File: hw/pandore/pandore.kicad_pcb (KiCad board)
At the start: 4 copper layers, 260 x 110 mm, 515 parts, among them J1 HDMI, J10 MIDI_in, J11 MIDI_out, J12 TRS, J13 NGFF_M.2_M, J14 VIN, J15 AIO, J16 DIO, J17 GROVE, J18 GROVE, J19 NGFF_M.2_AE, J2 USB2-A_2stacked, J20 V5, J21 V3.3, J22 V12ISO, J23 AV5, J24 AV3P3, J26 PPWR, J3 USB3-A_2stacked, J4 XLR+TRS6.35+3SW, J5 XLR+TRS6.35+3SW, J6 VIN, J7 TRS, J8 8p8c_2led_shield, J9 8p8c_2led_shield, M2AE30 M2, M2M110 M2, M2M42 M2, M2M60 M2, M2M80 M2, Q1 MOSFET_EN-N, Q2 MOSFET_EN-N, Q3 MOSFET_EN-N, Q4 MOSFET_EN-N, Q5 MOSFET_EN-N, Q6 MOSFET_EN-N, Q7 MOSFET_EN-N, T1 tran_choke_center, T10 tran_choke_center, T11 tran_choke_center, T12 tran_choke_center, T13 tran_choke_center, T14 tran_choke_center, T15 tran_choke_center, T16 tran_choke_center, T2 tran_choke_center, T3 tran_choke_center, T4 tran_choke_center, T5 tran_choke_center, T6 tran_choke_center, T7 tran_choke_center, T8 tran_choke_center, T9 tran_choke_center, U1 LattePanda_Mu, U10 H11L1, U11 CS4272, U12 NXES2, U13 LDL212DR, U14 LDL212DR, U15 OPAMP_DIFF_1, U16 OPAMP_DIFF_1, U17 OPAMP_DIFF_1, U18 OPAMP_DIFF_1, U19 AP6335xQ, U2 mem_flash_spi, U20 AP6335xQ, U21 LM5158, U22 TPS7A4001, U3 RP2350B, U4 RP2350B, U5 mem_flash_spi, U6 mem_flash_spi, U7 RTL8111H, U8 RTL8111H, U9 Teensy 4.1, X1 12MHz, 30ppm+30ppm, 10pF, X2 12MHz, 30ppm+30ppm, 10pF, X3 25MHz, 30ppm+30ppm, 10pF, X4 25MHz, 30ppm+30ppm, 10pF, X5 24.576MHz, 50ppm+20ppm, 18pF

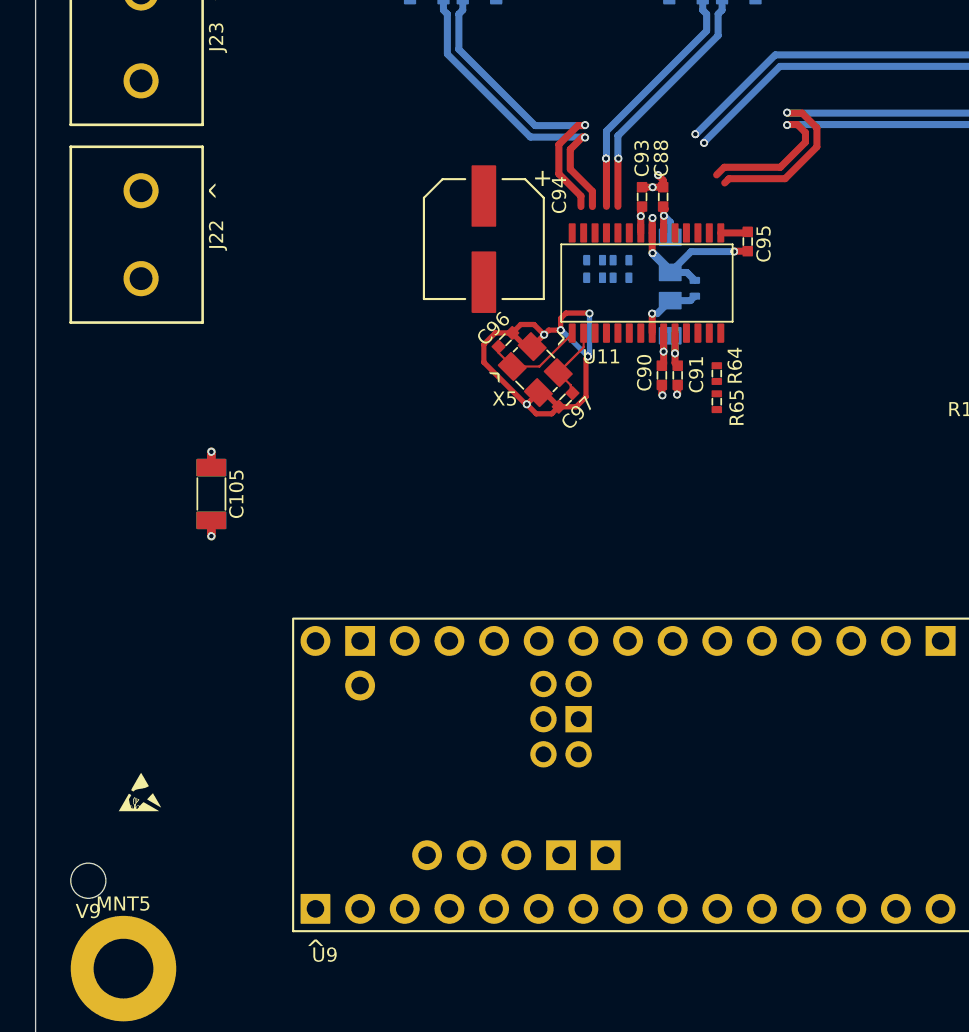
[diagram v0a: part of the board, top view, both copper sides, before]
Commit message: added i2s/i2c isolation for audio section
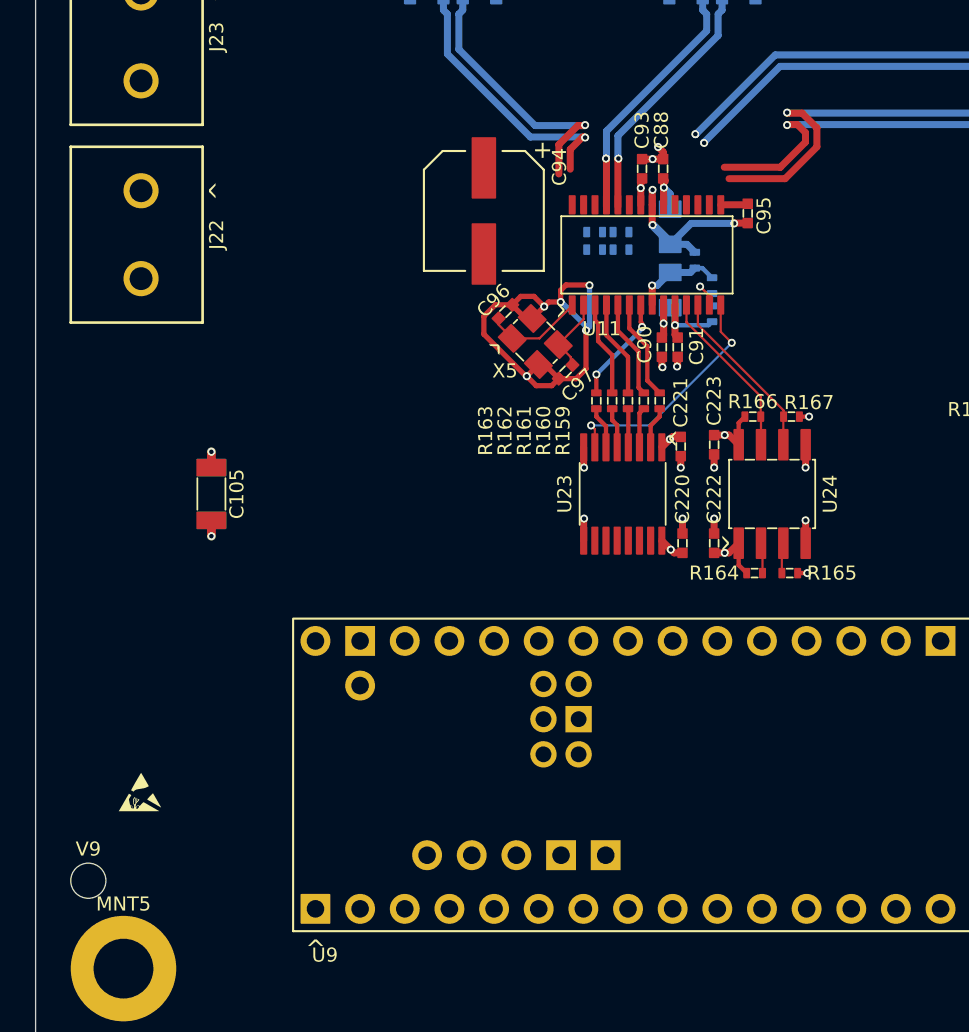
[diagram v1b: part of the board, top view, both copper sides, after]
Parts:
- added C220: 100nF, 16V, X7R, reekilib_cap:CAPC1005, F.Cu at (56.8, 120.8)
- added C221: 100nF, 16V, X7R, reekilib_cap:CAPC1005, F.Cu at (56.7, 115.3)
- added C222: 100nF, 16V, X7R, reekilib_cap:CAPC1005, F.Cu at (58.6, 120.8)
- added C223: 100nF, 16V, X7R, reekilib_cap:CAPC1005, F.Cu at (58.6, 115.2)
- added R159: 49.9Ω, 1%, 63mW, reekilib_res:RESC1005, F.Cu at (55.5, 112.7)
- added R160: 49.9Ω, 1%, 63mW, reekilib_res:RESC1005, F.Cu at (54.6, 112.7)
- added R161: 49.9Ω, 1%, 63mW, reekilib_res:RESC1005, F.Cu at (53.7, 112.7)
- added R162: 49.9Ω, 1%, 63mW, reekilib_res:RESC1005, F.Cu at (52.8, 112.7)
- added R163: 49.9Ω, 1%, 63mW, reekilib_res:RESC1005, F.Cu at (51.9, 112.7)
- added R164: 2.2kΩ, 1%, 63mW, reekilib_res:RESC1005, F.Cu at (60.9, 122.5)
- added R165: 2.2kΩ, 1%, 63mW, reekilib_res:RESC1005, F.Cu at (62.9, 122.5)
- added R166: 2.2kΩ, 1%, 63mW, reekilib_res:RESC1005, F.Cu at (60.8, 113.6)
- added R167: 2.2kΩ, 1%, 63mW, reekilib_res:RESC1005, F.Cu at (63.0, 113.6)
- added U23: ISO7762, reekilib_sop:SOP635P600X490-16, F.Cu at (53.4, 118.0)
- added U24: ISO1640, reekilib_soic:SOIC127P600X150-8, F.Cu at (61.9, 118.0)
- R64, R65: moved to B.Cu
- moved R65 6.61 mm to (58.5, 106.2), turned to 90 degrees
- moved R64 3.41 mm to (58.5, 107.8), turned to 90 degrees
- moved C89 1.60 mm to (56.1, 102.8)
- moved C97 1.60 mm to (50.1, 111.0)
- moved R106 1.60 mm to (53.3, 103.1)
- moved R107 1.60 mm to (51.8, 103.1)
- moved R108 1.60 mm to (53.3, 104.1)
- moved R109 1.60 mm to (51.8, 104.1)
- moved C88 1.60 mm to (55.7, 99.5)
- moved C90 1.60 mm to (55.6, 109.7)
- moved C91 1.60 mm to (56.5, 109.7)
- moved C92 1.60 mm to (56.1, 106.4)
- moved C93 1.60 mm to (54.5, 99.5)
- moved C94 1.60 mm to (45.5, 101.9)
- moved C95 1.60 mm to (60.5, 102.0)
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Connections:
- R64 pad 1: AVIO -> AV3P3
- U11 pad 14: /Audio/CODEC/CTL.~{RST} -> /Audio/CODEC/~{RST}
- U9 pad 10: /Audio/CODEC/DATA.RXD0 -> /Audio/Isolation/MCU.RXD0
- U9 pad 37: /Audio/CODEC/CTL.~{RST} -> /Audio/Isolation/MCU.~{RST}
- U9 pad 40: /Audio/CODEC/CTL.SDA -> /Audio/AUDMST.SDA
- U9 pad 41: /Audio/CODEC/CTL.SCL -> /Audio/AUDMST.SCL
- U9 pad 42: /Audio/CODEC/DATA.TXFS -> /Audio/Isolation/MCU.TXFS
- U9 pad 43: /Audio/CODEC/DATA.TXCLK -> /Audio/Isolation/MCU.TXCLK
- U9 pad 45: /Audio/CODEC/DATA.MCLK -> /Audio/Isolation/MCU.MCLK
- U9 pad 9: /Audio/CODEC/DATA.TXD0 -> /Audio/Isolation/MCU.TXD0
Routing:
- net /Audio/CODEC/~{RST}: track 0.00 -> 13.7 mm, vias 0 -> 2
- net /Audio/CODEC/CTL.SCL: track 0.00 -> 9.98 mm
- net /Audio/CODEC/CTL.SDA: track 0.00 -> 9.71 mm
- net AV3P3: track 5.97 -> 13.4 mm, vias 2 -> 5
- net /Audio/CODEC/DATA.TXD0: track 0.00 -> 6.11 mm, vias 0 -> 2
- net /Audio/CODEC/DATA.RXD0: track 0.00 -> 5.71 mm
- net /Audio/CODEC/DATA.TXCLK: track 0.00 -> 5.61 mm
- net V3P3: track 0.00 -> 5.53 mm, vias 0 -> 3
- net /Audio/CODEC/DATA.TXFS: track 0.00 -> 5.51 mm
- net /Audio/CODEC/DATA.MCLK: track 0.00 -> 5.40 mm
- net VSSISO: track 145.7 -> 150.8 mm, vias 58 -> 62
- net VSS: track 213.1 -> 217.4 mm, vias 83 -> 87
- net Net-(U11-AD0): track 0.00 -> 2.79 mm, vias 0 -> 1
- net /Audio/Audio outputs/RIGHT.SIG+: track 18.3 -> 15.6 mm
- net Net-(U23-OUTE): track 0.00 -> 2.42 mm
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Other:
- board text removed: "TODO: change M.2s for higher Z"
